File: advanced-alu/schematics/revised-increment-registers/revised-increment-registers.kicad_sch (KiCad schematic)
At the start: 13 parts

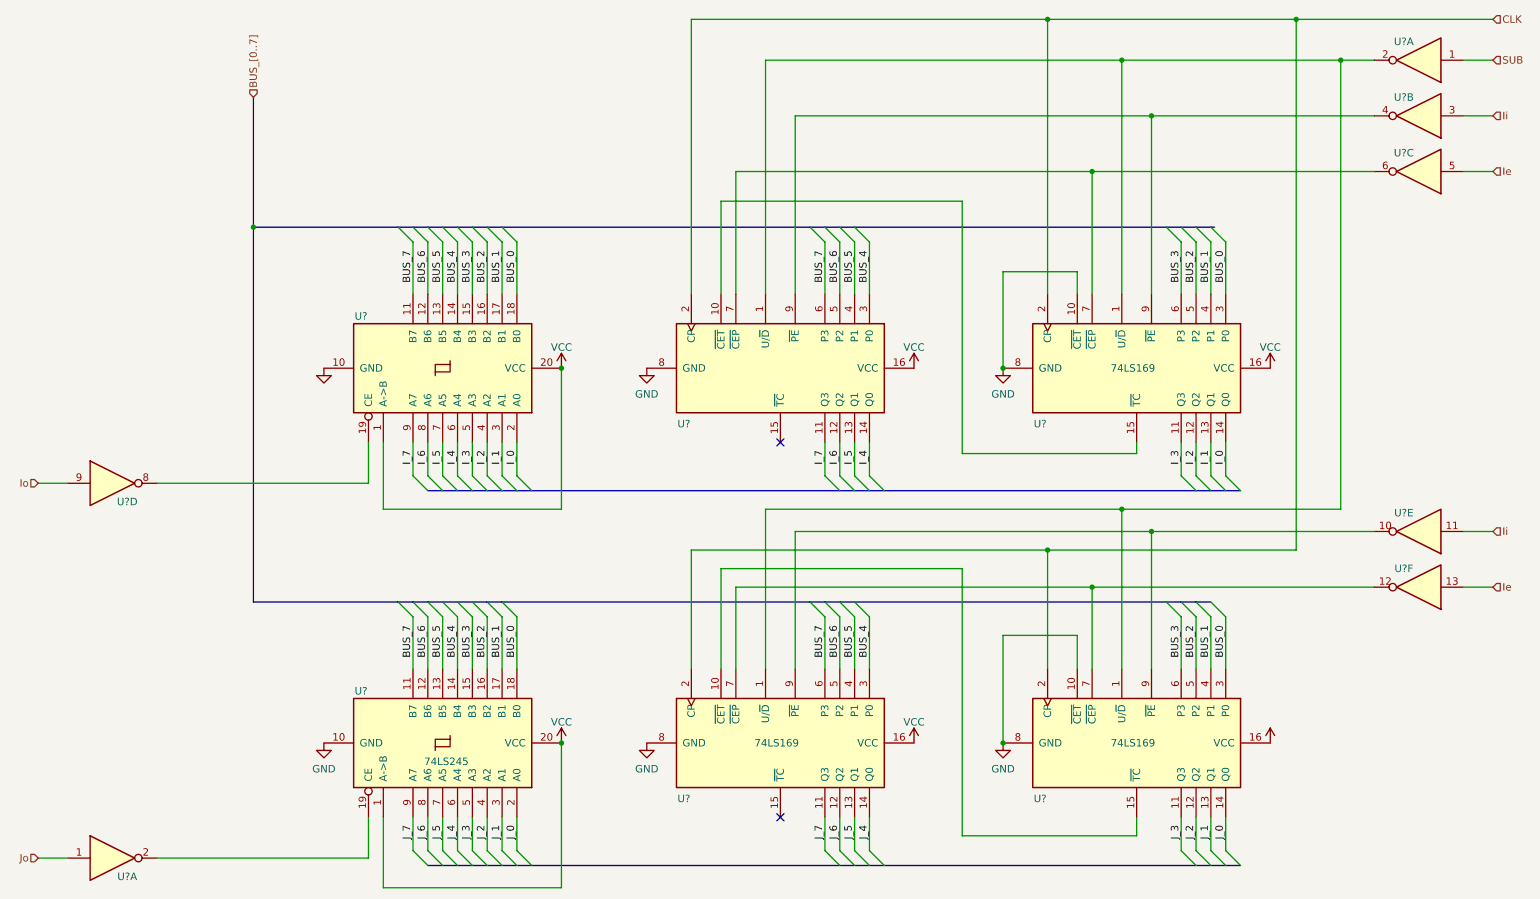
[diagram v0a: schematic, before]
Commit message: fixed label notation
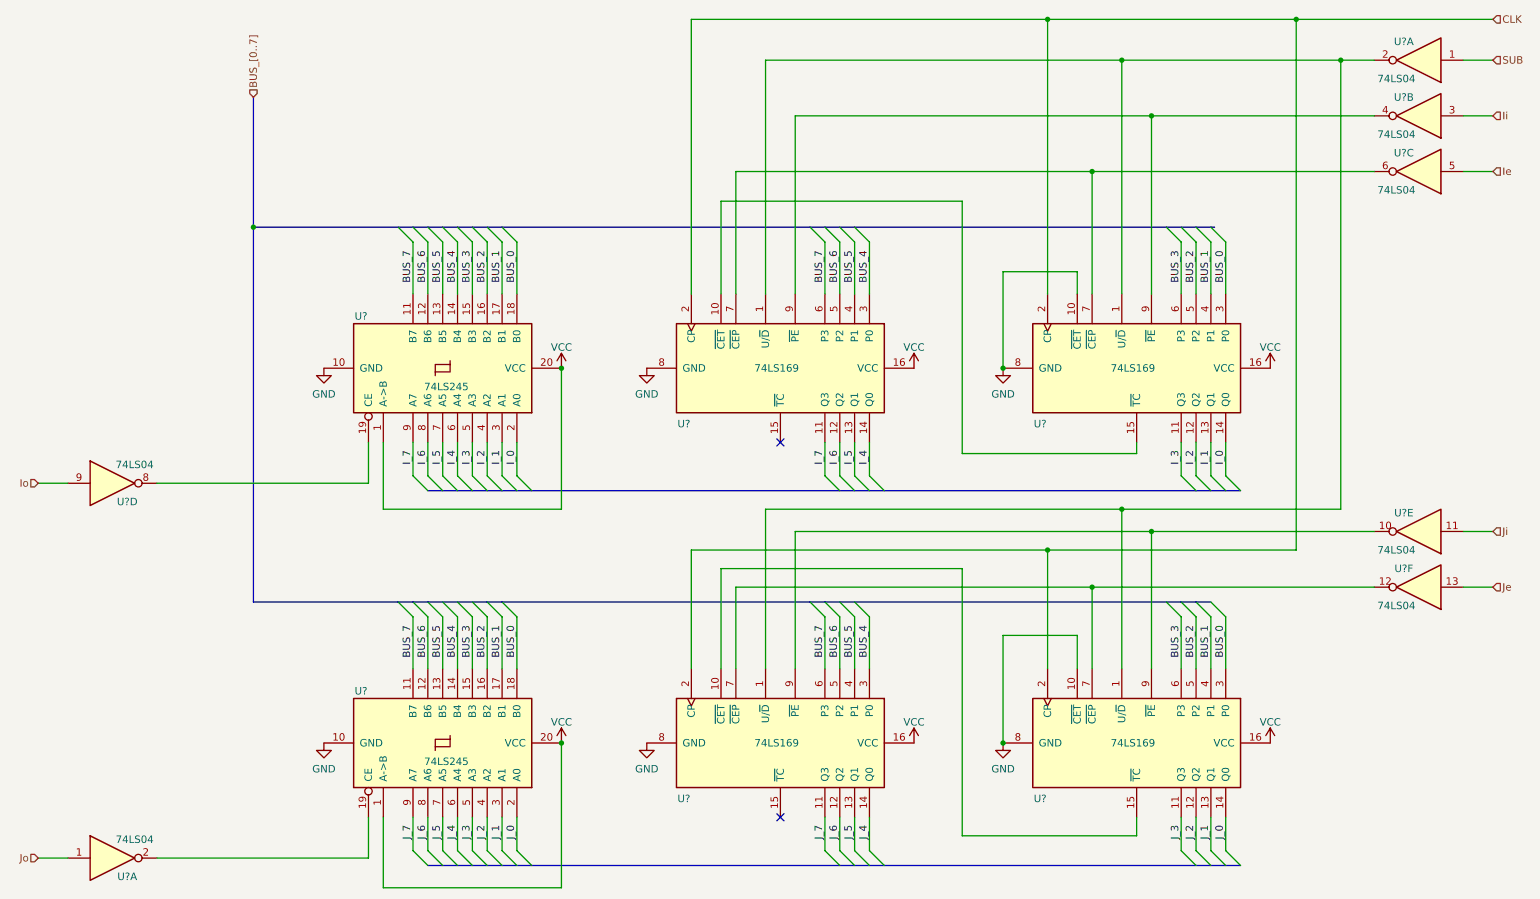
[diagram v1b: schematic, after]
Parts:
- U? (x7): value (none) -> 74LS04
- U?: value (none) -> 74LS169
- U?: value (none) -> 74LS245
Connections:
- net Ie: no longer U?.13
- net Ii: no longer U?.11
- new net Je: U?.13
- new net Ji: U?.11
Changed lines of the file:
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@@
     (effects (font (size 1.27 1.27)) (justify left bottom))
   )
-  (hierarchical_label "Ie" (shape input) (at 269.24 114.935 0)
+  (hierarchical_label "Je" (shape input) (at 269.24 114.935 0)
     (effects (font (size 1.27 1.27)) (justify left))
   )
@@
     (effects (font (size 1.27 1.27)) (justify right))
   )
-  (hierarchical_label "Ii" (shape input) (at 269.24 105.41 0)
+  (hierarchical_label "Ji" (shape input) (at 269.24 105.41 0)
     (effects (font (size 1.27 1.27)) (justify left))
   )
@@
     (in_bom yes) (on_board yes)
     (property "Reference" "U?" (id 0) (at 254 102.235 0))
-    (property "Value" "" (id 1) (at 252.73 108.585 0))
+    (property "Value" "74LS04" (id 1) (at 252.73 108.585 0))
     (property "Footprint" "" (id 2) (at 256.54 105.41 0)
       (effects (font (size 1.27 1.27)) hide)
@@
     (in_bom yes) (on_board yes)
     (property "Reference" "U?" (id 0) (at 35.56 100.33 0))
-    (property "Value" "" (id 1) (at 36.83 93.98 0))
+    (property "Value" "74LS04" (id 1) (at 36.83 93.98 0))
     (property "Footprint" "" (id 2) (at 33.02 97.155 0)
       (effects (font (size 1.27 1.27)) hide)
@@
     (in_bom yes) (on_board yes)
     (property "Reference" "U?" (id 0) (at 254 21.59 0))
-    (property "Value" "" (id 1) (at 252.73 27.94 0))
+    (property "Value" "74LS04" (id 1) (at 252.73 27.94 0))
     (property "Footprint" "" (id 2) (at 256.54 24.765 0)
       (effects (font (size 1.27 1.27)) hide)
@@
     (in_bom yes) (on_board yes)
     (property "Reference" "U?" (id 0) (at 254 111.76 0))
-    (property "Value" "" (id 1) (at 252.73 118.11 0))
+    (property "Value" "74LS04" (id 1) (at 252.73 118.11 0))
     (property "Footprint" "" (id 2) (at 256.54 114.935 0)
       (effects (font (size 1.27 1.27)) hide)
@@
       (effects (font (size 1.27 1.27)) hide)
     )
-    (property "Value" "" (id 1) (at 231.14 138.0292 0))
+    (property "Value" "VCC" (id 1) (at 231.14 138.0292 0))
     (property "Footprint" "" (id 2) (at 231.14 141.605 0)
       (effects (font (size 1.27 1.27)) hide)
@@
     (in_bom yes) (on_board yes)
     (property "Reference" "U?" (id 0) (at 35.56 164.465 0))
-    (property "Value" "" (id 1) (at 36.83 158.115 0))
+    (property "Value" "74LS04" (id 1) (at 36.83 158.115 0))
     (property "Footprint" "" (id 2) (at 33.02 161.29 0)
       (effects (font (size 1.27 1.27)) hide)
@@
     (in_bom yes) (on_board yes)
     (property "Reference" "U?" (id 0) (at 130.81 86.995 90))
-    (property "Value" "" (id 1) (at 146.685 77.47 90))
+    (property "Value" "74LS169" (id 1) (at 146.685 77.47 90))
     (property "Footprint" "" (id 2) (at 147.32 77.47 0)
       (effects (font (size 1.27 1.27)) hide)
@@
       (effects (font (size 1.27 1.27)) hide)
     )
-    (property "Value" "" (id 1) (at 69.215 81.9134 0))
+    (property "Value" "GND" (id 1) (at 69.215 81.9134 0))
     (property "Footprint" "" (id 2) (at 69.215 77.47 0)
       (effects (font (size 1.27 1.27)) hide)
@@
     (in_bom yes) (on_board yes)
     (property "Reference" "U?" (id 0) (at 75.565 68.58 90))
-    (property "Value" "" (id 1) (at 90.17 80.645 90))
+    (property "Value" "74LS245" (id 1) (at 90.17 80.645 90))
     (property "Footprint" "" (id 2) (at 89.535 77.47 0)
       (effects (font (size 1.27 1.27)) hide)
@@
     (in_bom yes) (on_board yes)
     (property "Reference" "U?" (id 0) (at 254 31.115 0))
-    (property "Value" "" (id 1) (at 252.73 37.465 0))
+    (property "Value" "74LS04" (id 1) (at 252.73 37.465 0))
     (property "Footprint" "" (id 2) (at 256.54 34.29 0)
       (effects (font (size 1.27 1.27)) hide)
@@
     (in_bom yes) (on_board yes)
     (property "Reference" "U?" (id 0) (at 254 40.64 0))
-    (property "Value" "" (id 1) (at 252.73 46.99 0))
+    (property "Value" "74LS04" (id 1) (at 252.73 46.99 0))
     (property "Footprint" "" (id 2) (at 256.54 43.815 0)
       (effects (font (size 1.27 1.27)) hide)
